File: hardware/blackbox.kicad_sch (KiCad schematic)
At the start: 3 parts, among them U13 PY25Q128HA-DFH-IR

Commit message: Trim BOM to strictly needed parts, fill sourcing fields, fix library datasheets
Owner review 2026-10-11, schematic only (board not resynced).

Removed (17 parts): D1 TVS (clamps above every IC abs max), R2/R3/C5
INA186 input RC, U5 TPS22810 O4 switch with C16/C129/R9/R10/R87/D2
(VHD pad now on +5V_BST, as Matrix HD boards; HD_EN still holds the
analog VTX off via Q28, R11 kept), R67 selector (PA_VCC is +BATT),
TH1/R70 PA NTC and R84 (patched-ELRS only; GPIO37/GPIO4 no-connect),
C92 and C121 (beyond SX1281 / LP5912 datasheet decoupling).

Changed: D4 WS2812 VDD to +5V (3.5 V min); X3 TCXO pin 1 floating per
the YXC sheet; C122/C123/C134 4.7 uF 0402 -> 0201 GRM035R60J475ME15D.

Sourcing: LCSC numbers for 21 MPN lines (SKUBAAE010 has no listing);
every BOM part keeps MPN + Manufacturer for NextPCB.

Library: 16 unused lib symbols pruned; dead or HTML-only datasheet
links replaced with verified PDF URLs (RTC6705, SE5004L, FL2, X1,
EFM8BB51, BC857BM, FTC252012, HCS1206 shunt, Molex 53047).

Net-class patterns and contract entries for the removed nets dropped;
PINMAP ESP32 rows updated (GPIO36 is ADC1_CH0).

Validation: ERC 0 errors / 2 warnings (baseline); check_netlist 7 ok;
sch_integrate --check idempotent; check_conventions unchanged.

Co-Authored-By: Claude Opus 5.5 <noreply@anthropic.com>
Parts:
- U13: LCSC (none) -> C53467986
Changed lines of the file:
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@@
 		(in_pos_files no)
 		(dnp no)
-		(property "Reference" "#PWR144"
+		(property "Reference" "#PWR135"
 			(at 96.52 77.47 0)
 			(hide yes)
@@
 			(project "OpenAIO-Whoop"
 				(path "/2c3a7206-1e66-4d43-a02f-491225e20dd6/04f14c5a-8e46-5d66-be84-2bb8762684a3"
-					(reference "#PWR144")
+					(reference "#PWR135")
 					(unit 1)
 				)
@@
 		(in_pos_files no)
 		(dnp no)
-		(property "Reference" "#PWR143"
+		(property "Reference" "#PWR134"
 			(at 83.82 60.96 0)
 			(hide yes)
@@
 			(project "OpenAIO-Whoop"
 				(path "/2c3a7206-1e66-4d43-a02f-491225e20dd6/04f14c5a-8e46-5d66-be84-2bb8762684a3"
-					(reference "#PWR143")
+					(reference "#PWR134")
 					(unit 1)
 				)
@@
 		(in_pos_files no)
 		(dnp no)
-		(property "Reference" "#PWR142"
+		(property "Reference" "#PWR133"
 			(at 53.34 57.15 0)
 			(hide yes)
@@
 			(project "OpenAIO-Whoop"
 				(path "/2c3a7206-1e66-4d43-a02f-491225e20dd6/04f14c5a-8e46-5d66-be84-2bb8762684a3"
-					(reference "#PWR142")
+					(reference "#PWR133")
 					(unit 1)
 				)
@@
 		(in_pos_files no)
 		(dnp no)
-		(property "Reference" "#PWR145"
+		(property "Reference" "#PWR136"
 			(at 74.93 87.63 0)
 			(hide yes)
@@
 			(project "OpenAIO-Whoop"
 				(path "/2c3a7206-1e66-4d43-a02f-491225e20dd6/04f14c5a-8e46-5d66-be84-2bb8762684a3"
-					(reference "#PWR145")
+					(reference "#PWR136")
 					(unit 1)
 				)
@@
 		(in_pos_files no)
 		(dnp no)
-		(property "Reference" "#PWR141"
+		(property "Reference" "#PWR132"
 			(at 76.2 48.26 0)
 			(hide yes)
@@
 			(project "OpenAIO-Whoop"
 				(path "/2c3a7206-1e66-4d43-a02f-491225e20dd6/04f14c5a-8e46-5d66-be84-2bb8762684a3"
-					(reference "#PWR141")
+					(reference "#PWR132")
 					(unit 1)
 				)
@@
 			)
 		)
-		(property "LCSC" ""
+		(property "LCSC" "C53467986"
 			(at 76.2 68.58 0)
 			(hide yes)

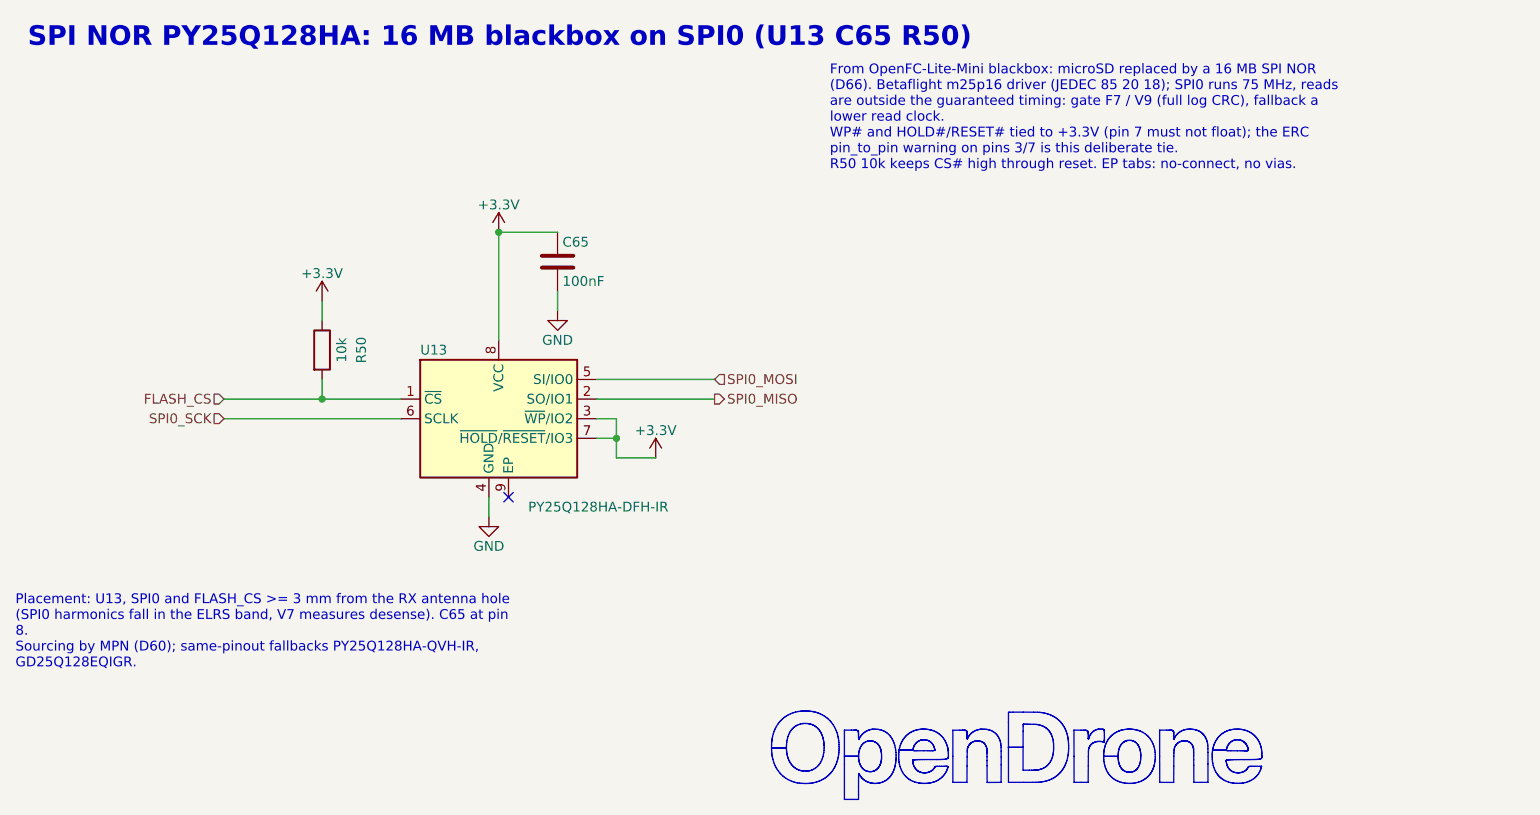
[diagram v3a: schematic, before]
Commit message: Footprint audit vs datasheets, 0201 lands to Murata minimum, schematic notes shortened
Footprints: 45 checked against their datasheets by group, no pin or
land errors. C/R/L_0201_..._L pad height 0.28 -> 0.30 (Murata GRM03
reflow table c >= 0.30); other lands already at least density per D109
and left unchanged. Land spec texts cleaned (sources, shared parts).

Schematic notes: 157 -> 152 items, 19.5k -> 9.7k characters, all
current (diode-OR, removed parts, RTC6705 filters, TX0/RX0).

check_footprint 107/107 lib specs PASS; ERC 0 errors / 2 warnings;
check_netlist 7 ok; sch_integrate --check clean. Board not synced.

Co-Authored-By: Claude Opus 5.5 <noreply@anthropic.com>
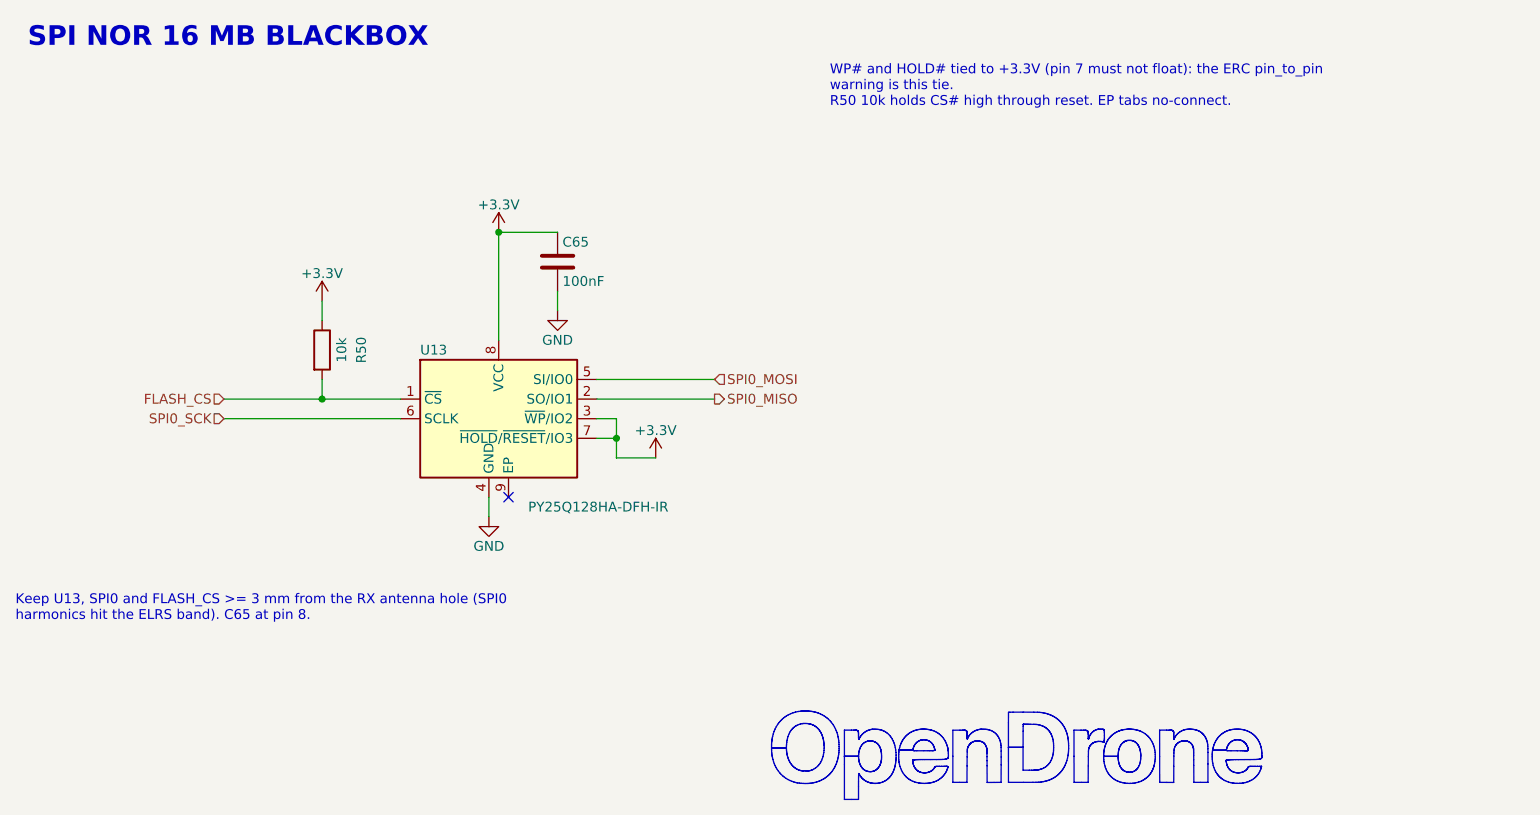
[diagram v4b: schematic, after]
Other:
- note added: "SPI NOR 16 MB BLACKBOX"
- note removed: "SPI NOR PY25Q128HA: 16 MB blackbox on SPI0 (U13 C65 R50)"
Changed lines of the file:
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@@
 		)
 	)
-	(text "SPI NOR PY25Q128HA: 16 MB blackbox on SPI0 (U13 C65 R50)"
+	(text "SPI NOR 16 MB BLACKBOX"
 		(exclude_from_sim no)
 		(at 15.24 17.78 0)
@@
 		)
 	)
-	(text_box "Placement: U13, SPI0 and FLASH_CS >= 3 mm from the RX antenna hole (SPI0 harmonics fall in the ELRS band, V7 measures desense). C65 at pin 8.\nSourcing by MPN (D60); same-pinout fallbacks PY25Q128HA-QVH-IR, GD25Q128EQIGR."
+	(text_box "Keep U13, SPI0 and FLASH_CS >= 3 mm from the RX antenna hole (SPI0 harmonics hit the ELRS band). C65 at pin 8."
 		(exclude_from_sim no)
 		(at 12.7 90.17 0)
@@
 		)
 	)
-	(text_box "From OpenFC-Lite-Mini blackbox: microSD replaced by a 16 MB SPI NOR (D66). Betaflight m25p16 driver (JEDEC 85 20 18); SPI0 runs 75 MHz, reads are outside the guaranteed timing: gate F7 / V9 (full log CRC), fallback a lower read clock.\nWP# and HOLD#/RESET# tied to +3.3V (pin 7 must not float); the ERC pin_to_pin warning on pins 3/7 is this deliberate tie.\nR50 10k keeps CS# high through reset. EP tabs: no-connect, no vias."
+	(text_box "WP# and HOLD# tied to +3.3V (pin 7 must not float): the ERC pin_to_pin warning is this tie.\nR50 10k holds CS# high through reset. EP tabs no-connect."
 		(exclude_from_sim no)
 		(at 118.11 21.59 0)
